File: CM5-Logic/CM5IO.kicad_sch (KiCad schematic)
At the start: 19 parts, among them J10 691210910004, J2 B2B-PH-K-S, J3 B2B-PH-K-S, J4 VR10S09, J6 691210910006, J7 691210910006, J9 1726470103, U2 RCLAMP3354S.TCT

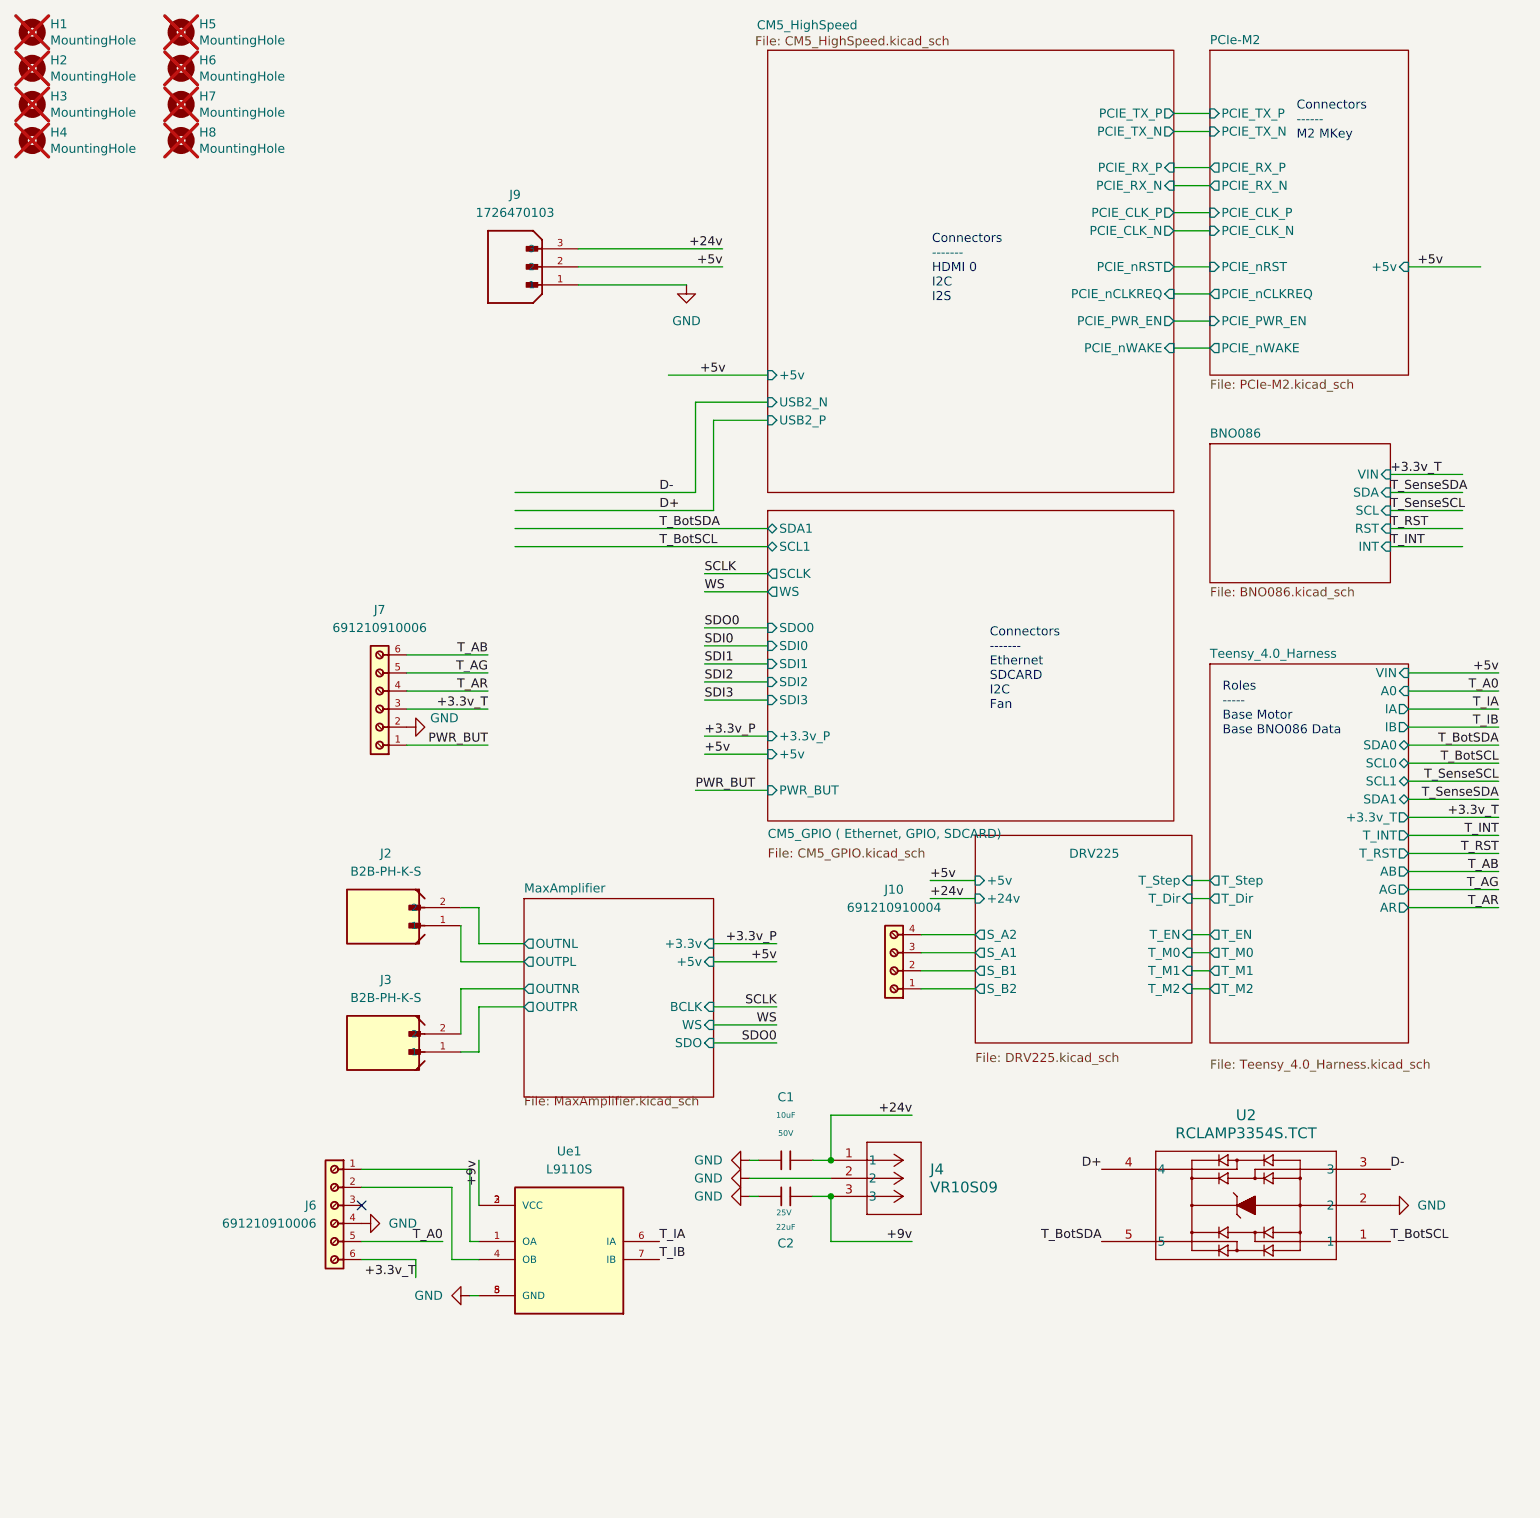
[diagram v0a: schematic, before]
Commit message: adds respeaker and reworks the amplifier
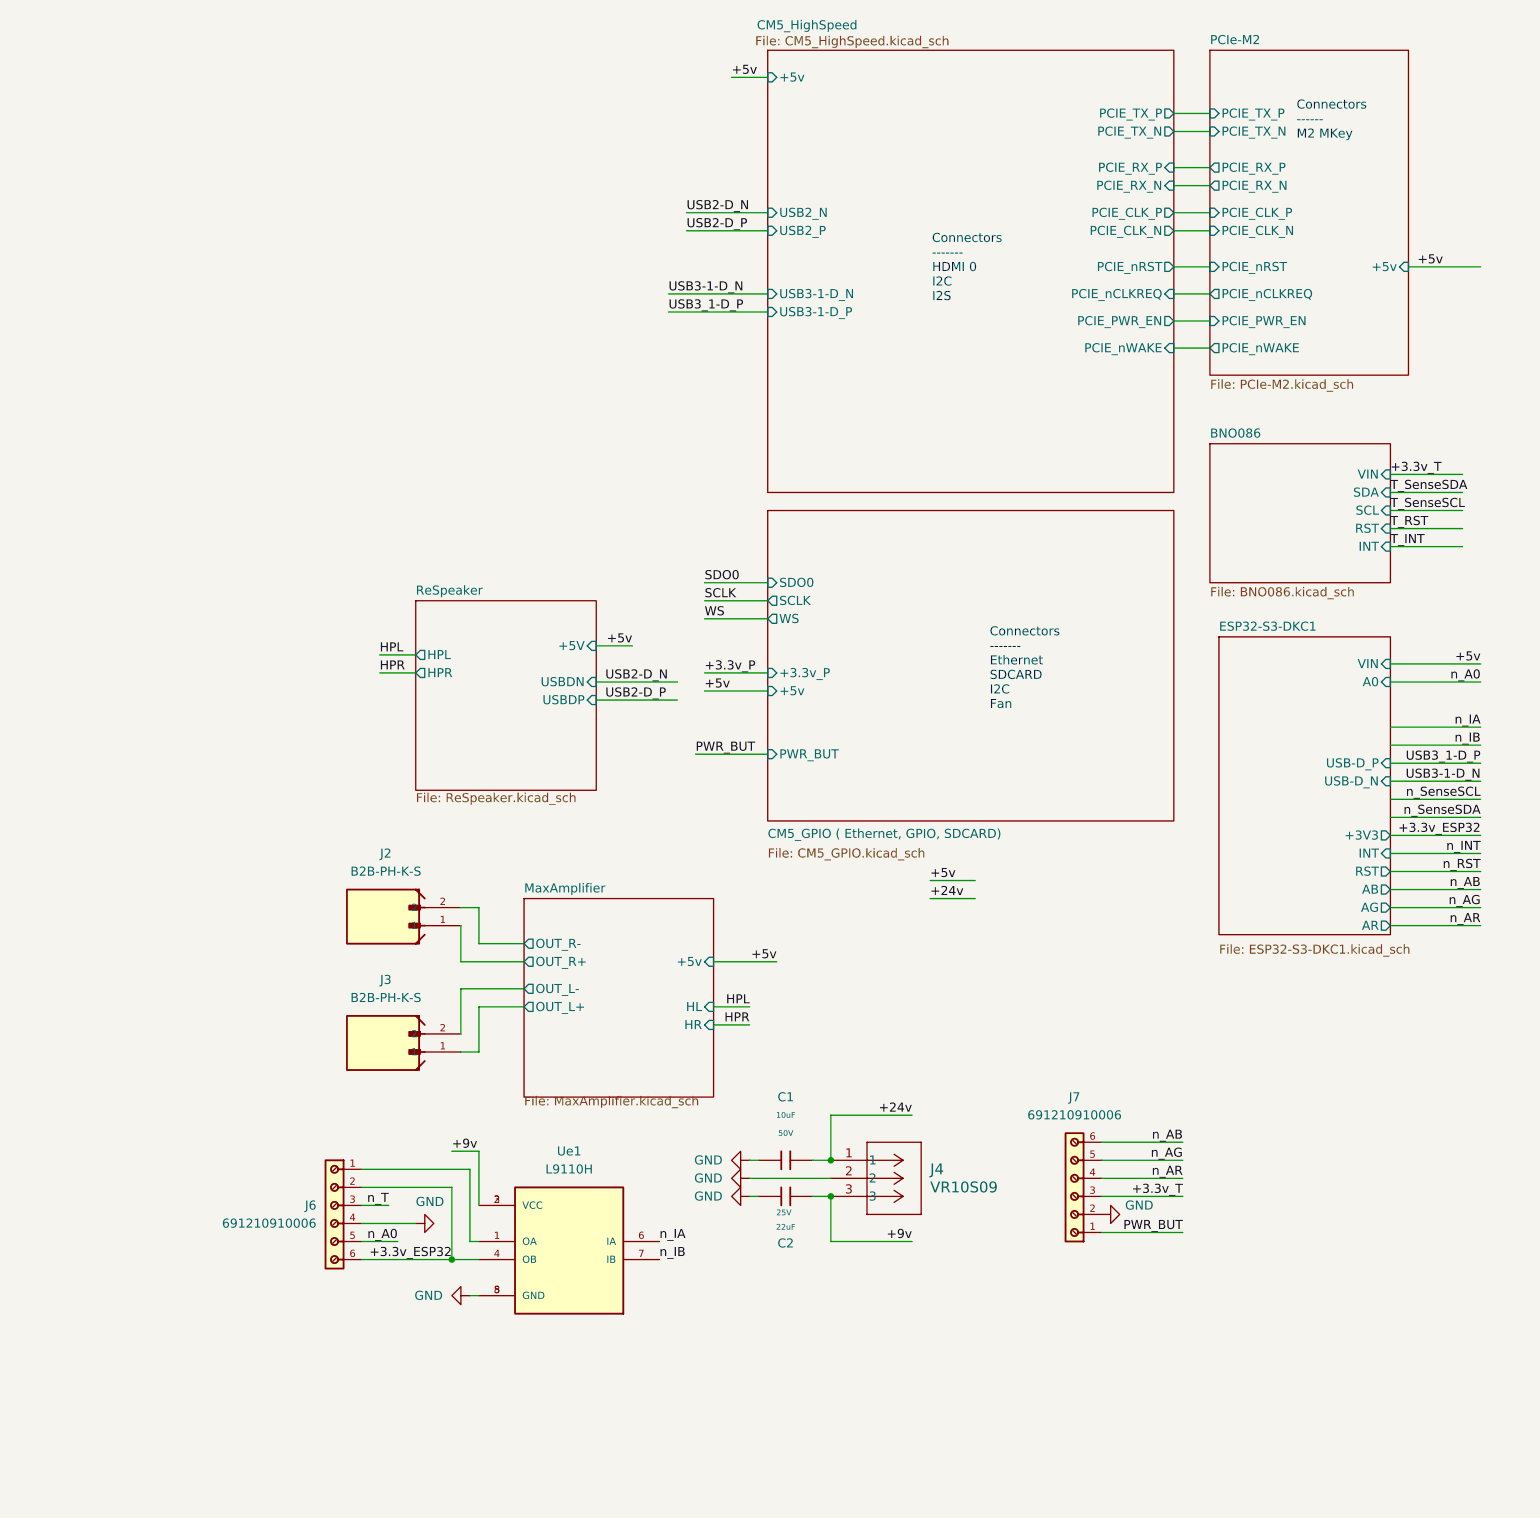
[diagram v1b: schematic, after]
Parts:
- removed H1, H2, H3, H4, H5, H6, H7, H8: MountingHole, CM5IO:MountingHole_2.7mm_M2.5_DIN965, symbol Mechanical:MountingHole
- removed J10: 691210910004, Custom Components:691210910004, symbol 691210910004:691210910004
- removed J9: 1726470103, Custom Components:MOLEX_1726470103, symbol 1726470103:1726470103
- removed U2: RCLAMP3354S.TCT, SOT-23-5L_SEM, symbol RCLAMP3354S_TCT:RCLAMP3354S.TCT
- Ue1: value L9110S -> L9110H
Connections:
- net +3.3v_T: no longer J6.6
- net +3.3v_ESP32: now reaches J6.2, Ue1.4 (OB)
- net +3.3v_ESP32: now also J6.6
- net n_T: now reaches J6.3
- net MaxAmplifier/OUTNL renamed MaxAmplifier/OUT_R-
- net MaxAmplifier/OUTNR renamed MaxAmplifier/OUT_L-
- net MaxAmplifier/OUTPL renamed MaxAmplifier/OUT_R+
- net MaxAmplifier/OUTPR renamed MaxAmplifier/OUT_L+
- net T_A0 renamed n_A0
- net T_AB renamed n_AB
- net T_AG renamed n_AG
- net T_AR renamed n_AR
- net T_IA renamed n_IA
- net T_IB renamed n_IB
- no-connect marks 1 -> 0
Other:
- removed sheet DRV225
- removed sheet Teensy_4.0_Harness
- added sheet ESP32-S3-DKC1 (ESP32-S3-DKC1.kicad_sch)
- added sheet ReSpeaker (ReSpeaker.kicad_sch)
- sheet CM5_GPIO ( Ethernet, GPIO, SDCARD) ports: added none; removed SCL1, SDA1, SDI0, SDI1, SDI2, SDI3
- sheet CM5_HighSpeed ports: added USB3-1-D_N, USB3-1-D_P; removed none
- sheet MaxAmplifier ports: added HL, HR, OUT_L+, OUT_L-, OUT_R+, OUT_R-; removed +3.3v, BCLK, OUTNL, OUTNR, OUTPL, OUTPR, SDO, WS
- note removed: "Roles ----- Base Motor Base BNO086 Data"
- moved on the sheet: J7

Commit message: adds power connector and works on the ESP32 outputs
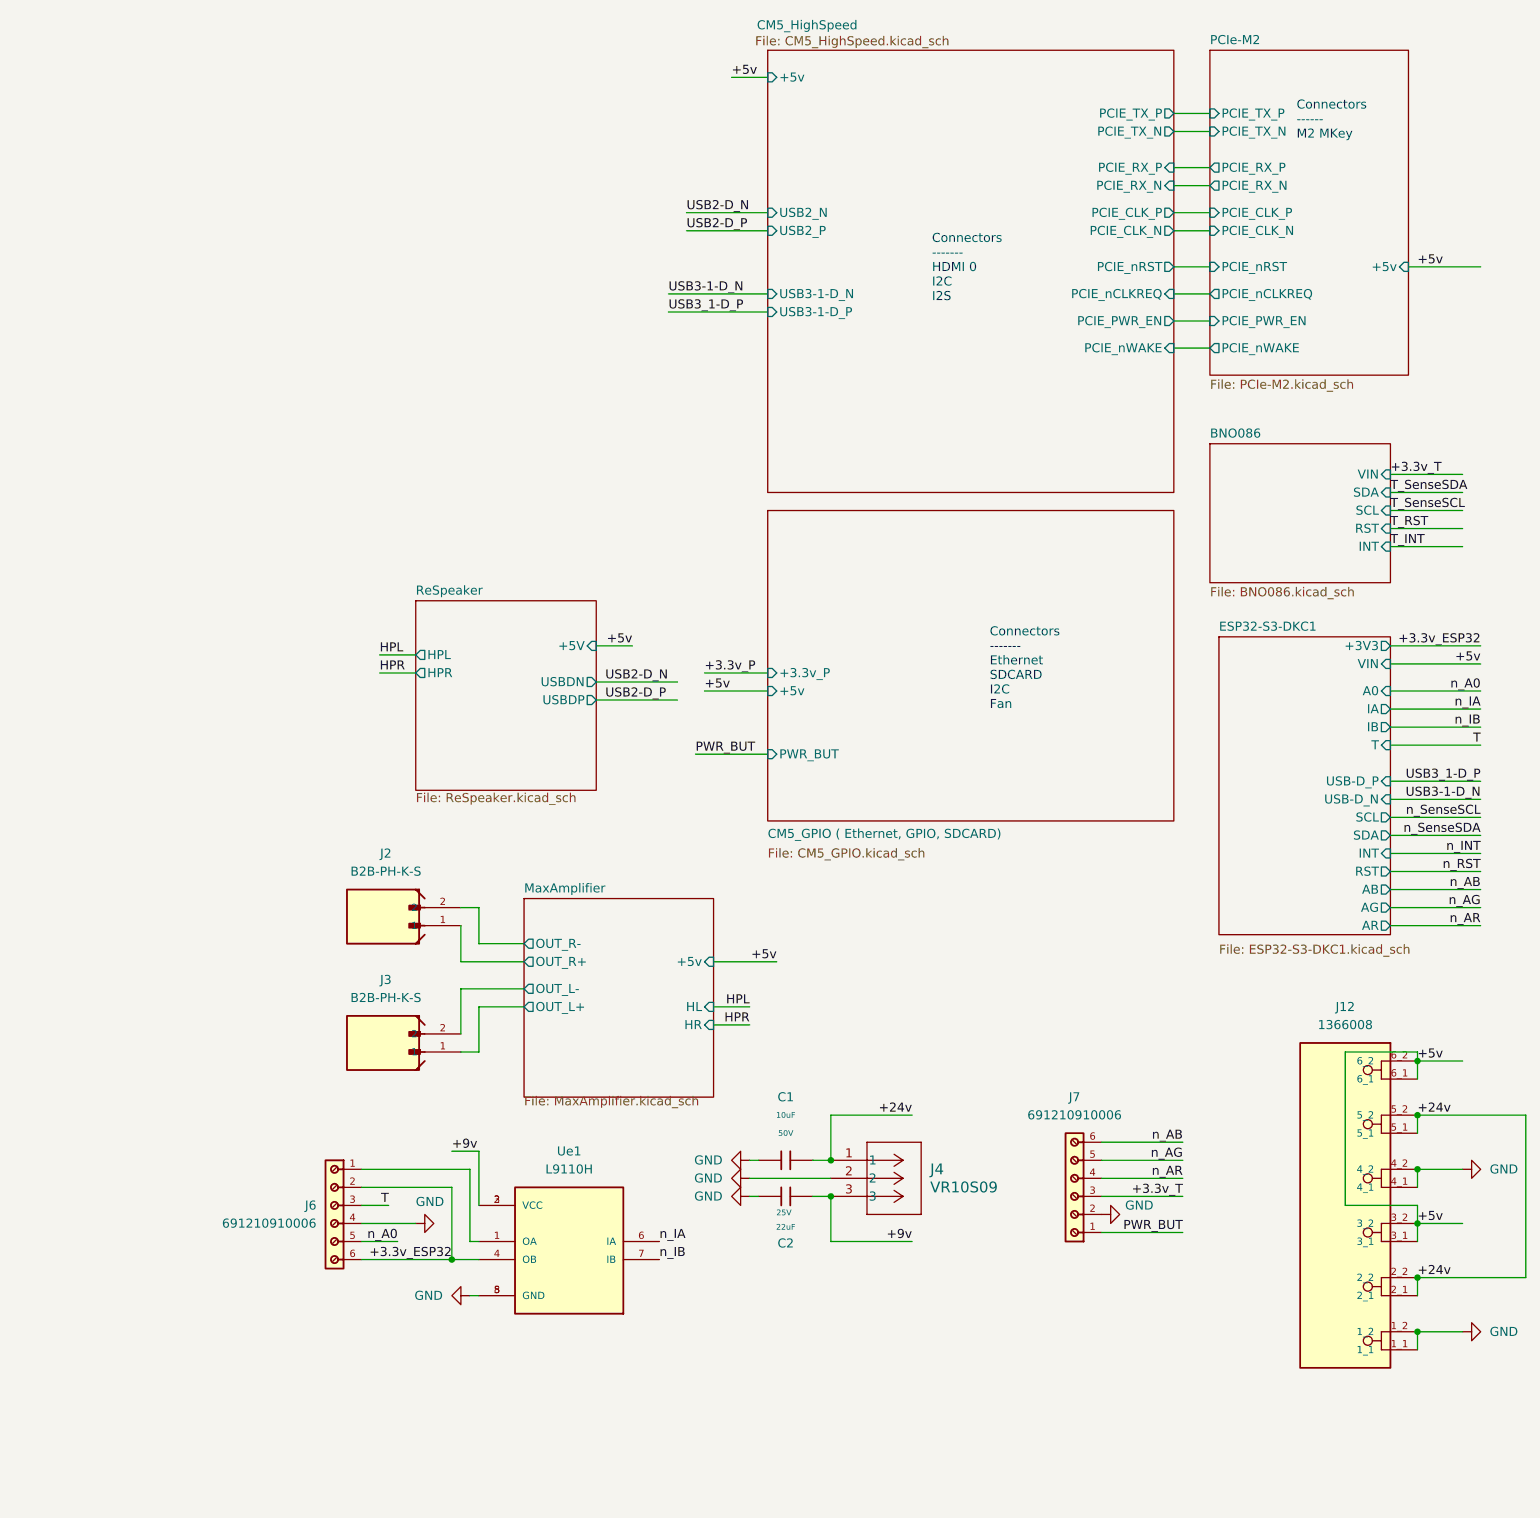
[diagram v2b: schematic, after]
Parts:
- added J12: 1366008, 1366008:PHOENIX_1366008, symbol 1366008:1366008
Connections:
- net +24v: now also J12.2_1, J12.2_2, J12.5_1, J12.5_2
- net +5v: now also J12.3_1, J12.3_2, J12.6_1, J12.6_2
- net GND: now also J12.1_1, J12.1_2, J12.4_1, J12.4_2
- net n_T renamed T
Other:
- sheet CM5_GPIO ( Ethernet, GPIO, SDCARD) ports: added none; removed SCLK, SDO0, WS
- sheet ESP32-S3-DKC1 ports: added IA, IB, SCL, SDA, T; removed none

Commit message: fixes a few label issues
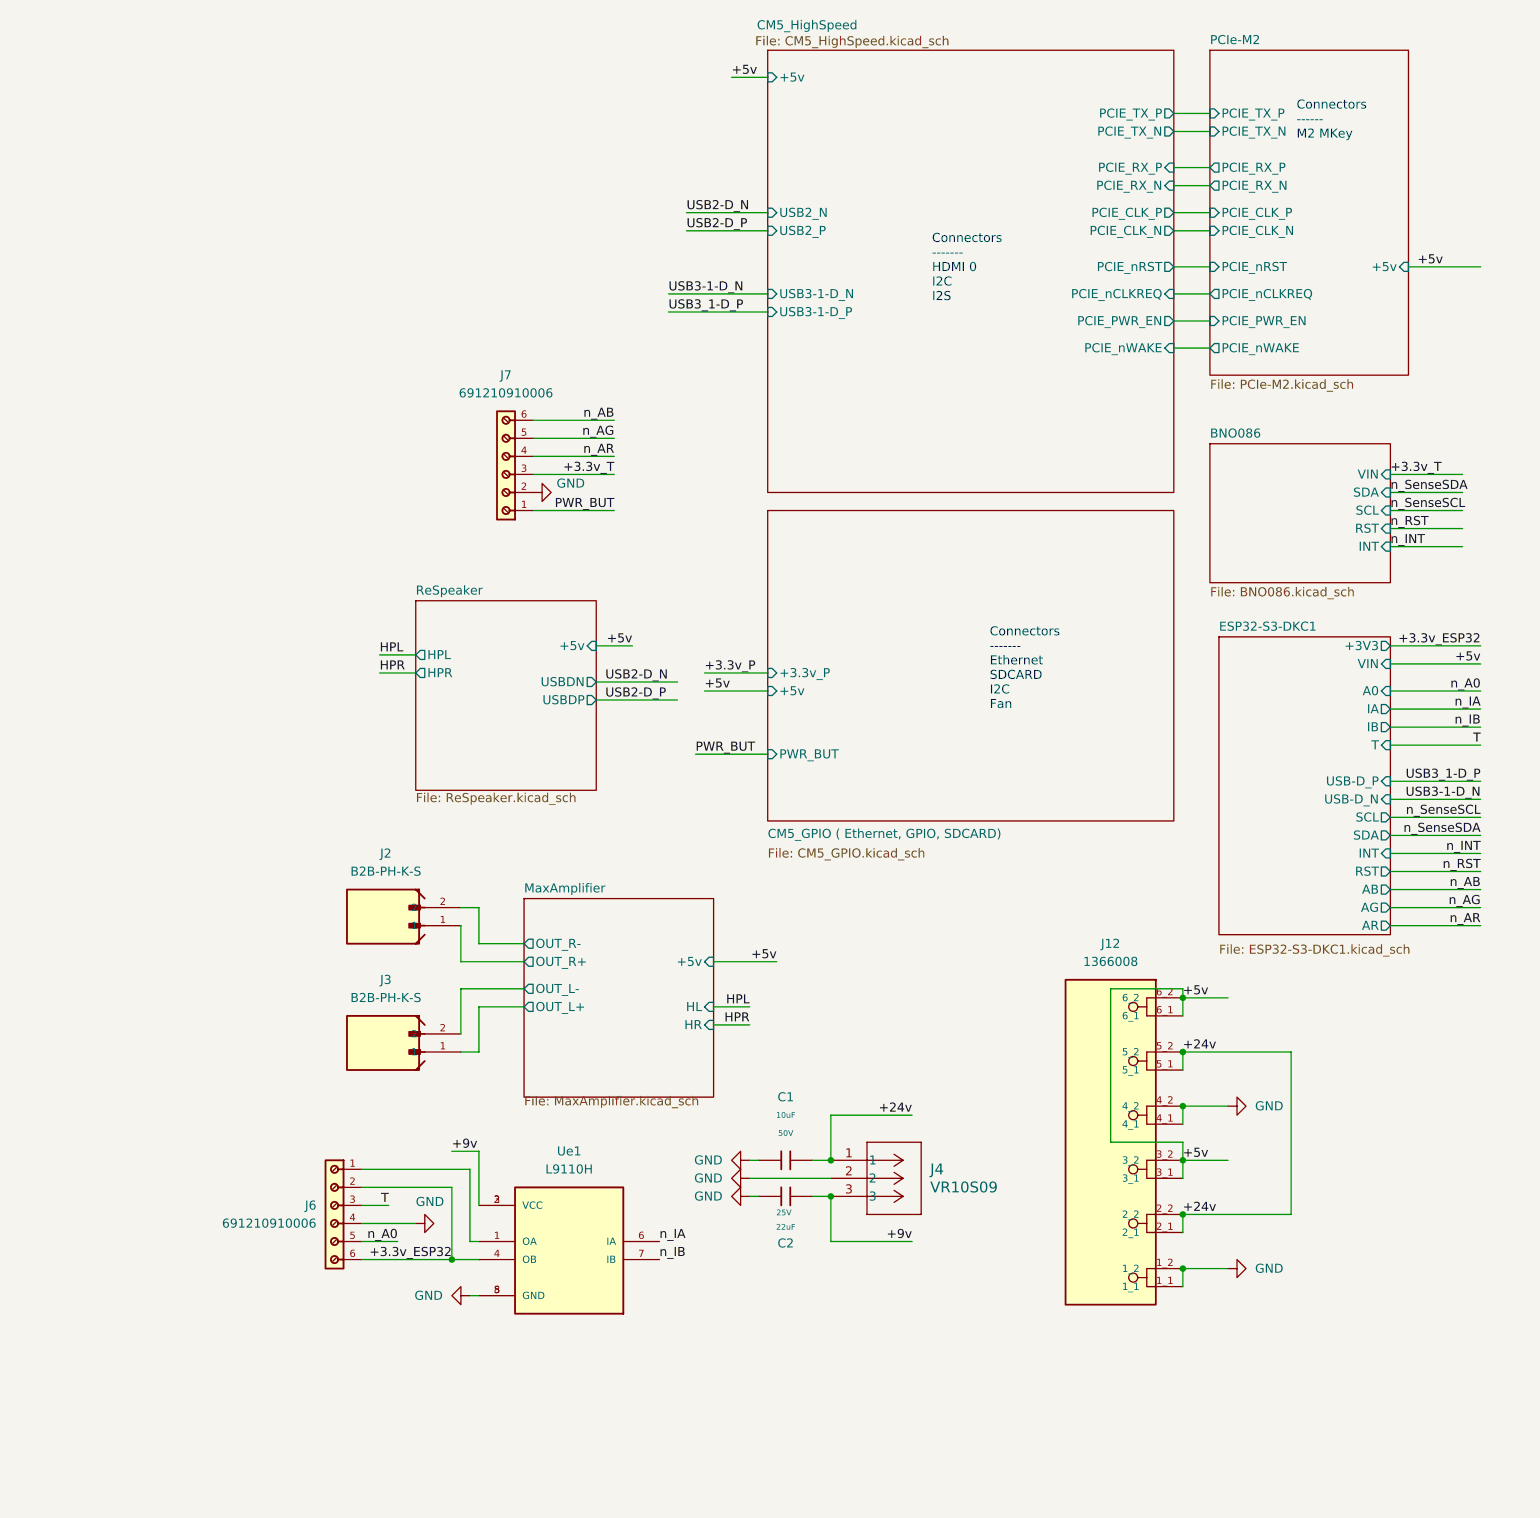
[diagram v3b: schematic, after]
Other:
- sheet ReSpeaker ports: added +5v; removed +5V
- moved on the sheet: J12, J7
